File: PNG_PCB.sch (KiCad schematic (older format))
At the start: 2 parts, among them U1 screw_term, U2 Teensy4.1

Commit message: updated screw terminals to 2.54mm
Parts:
- removed U1: screw_term, Connector_PinHeader_1.27mm:PinHeader_1x02_P1.27mm_Vertical, symbol PNG_PCB_Parts:screw_term
- added J91: screw terminal, Connector_PinHeader_2.54mm:PinHeader_1x02_P2.54mm_Vertical, symbol Connector:Conn_01x02_Male
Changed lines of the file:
@@
 Text Label 3250 6450 2    50   ~ 0
 ADC_IN_9
-Wire Wire Line
-	5000 3250 4400 3250
-Text Label 4400 3250 0    50   ~ 0
+Text Label 5900 4300 2    50   ~ 0
 sync_in
-$Comp
-L PNG_PCB_Parts:screw_term U1
-U 1 1 601BAD2F
-P 5000 3250
-F 0 "U1" H 5058 3384 50  0000 L CNN
-F 1 "screw_term" H 5058 3293 50  0000 L CNN
-F 2 "Connector_PinHeader_1.27mm:PinHeader_1x02_P1.27mm_Vertical" H 5000 3250 50  0001 C CNN
-F 3 "" H 5000 3250 50  0001 C CNN
-	1    5000 3250
-	1    0    0    -1
-$EndComp
 Wire Wire Line
 	7300 1750 6700 1750
 Text Label 6700 1750 0    50   ~ 0
 sync_out
-Wire Wire Line
-	5000 3600 4400 3600
-Text Label 4400 3600 0    50   ~ 0
+Text Label 5900 4200 2    50   ~ 0
 sync_out
-$Comp
-L PNG_PCB_Parts:screw_term U1
-U 2 1 601BD94C
-P 5000 3600
-F 0 "U1" H 5058 3734 50  0000 L CNN
-F 1 "screw_term" H 5058 3643 50  0000 L CNN
-F 2 "Connector_PinHeader_1.27mm:PinHeader_1x02_P1.27mm_Vertical" H 5000 3600 50  0001 C CNN
-F 3 "" H 5000 3600 50  0001 C CNN
-	2    5000 3600
-	1    0    0    -1
-$EndComp
 NoConn ~ 9500 2950
 NoConn ~ 9500 3050
@@
 NoConn ~ 9500 3850
 NoConn ~ 9500 3950
+$Comp
+L Connector:Conn_01x02_Male J91
+U 1 1 601A940A
+P 5050 4200
+F 0 "J91" H 5158 4381 50  0000 C CNN
+F 1 "screw terminal" H 5158 4290 50  0000 C CNN
+F 2 "Connector_PinHeader_2.54mm:PinHeader_1x02_P2.54mm_Vertical" H 5050 4200 50  0001 C CNN
+F 3 "~" H 5050 4200 50  0001 C CNN
+	1    5050 4200
+	1    0    0    -1
+$EndComp
+Wire Wire Line
+	5250 4200 5900 4200
+Wire Wire Line
+	5250 4300 5900 4300
 $EndSCHEMATC

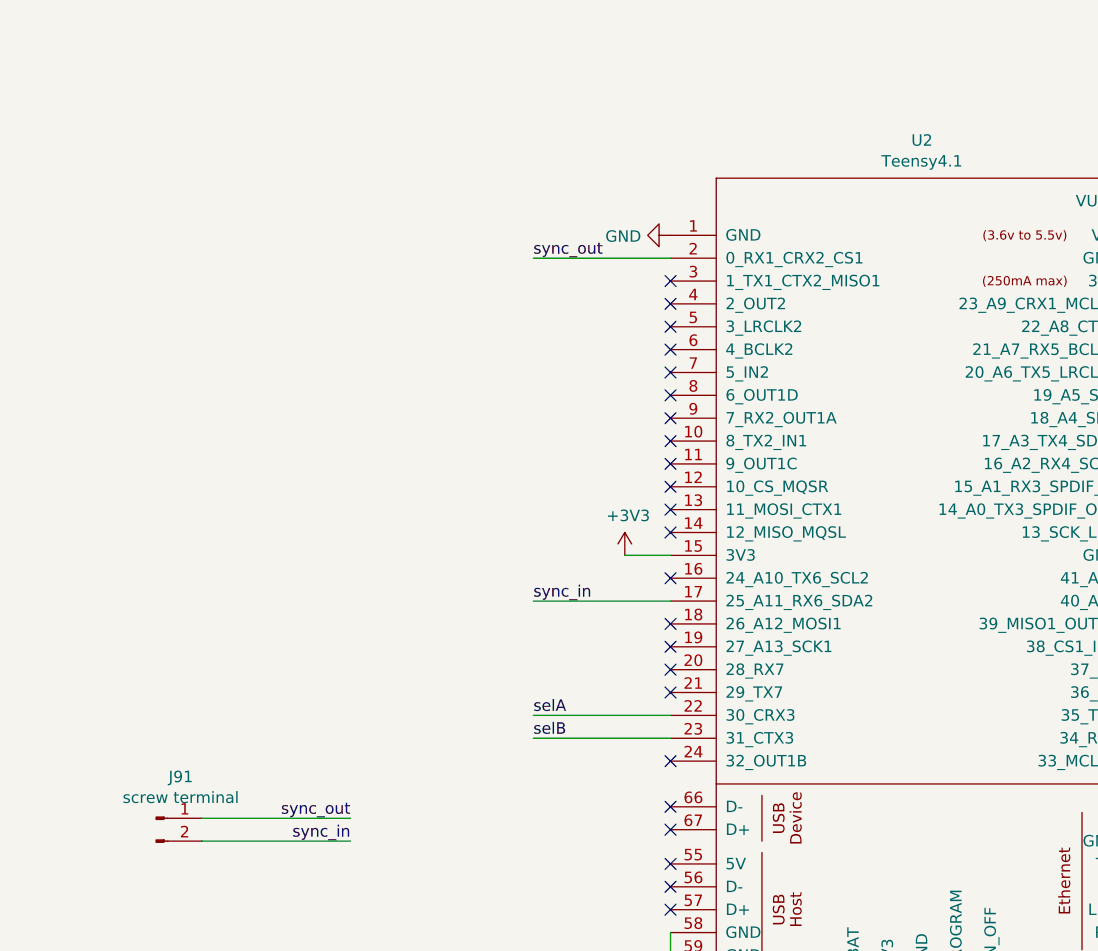
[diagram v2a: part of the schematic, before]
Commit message: revised sensor connector
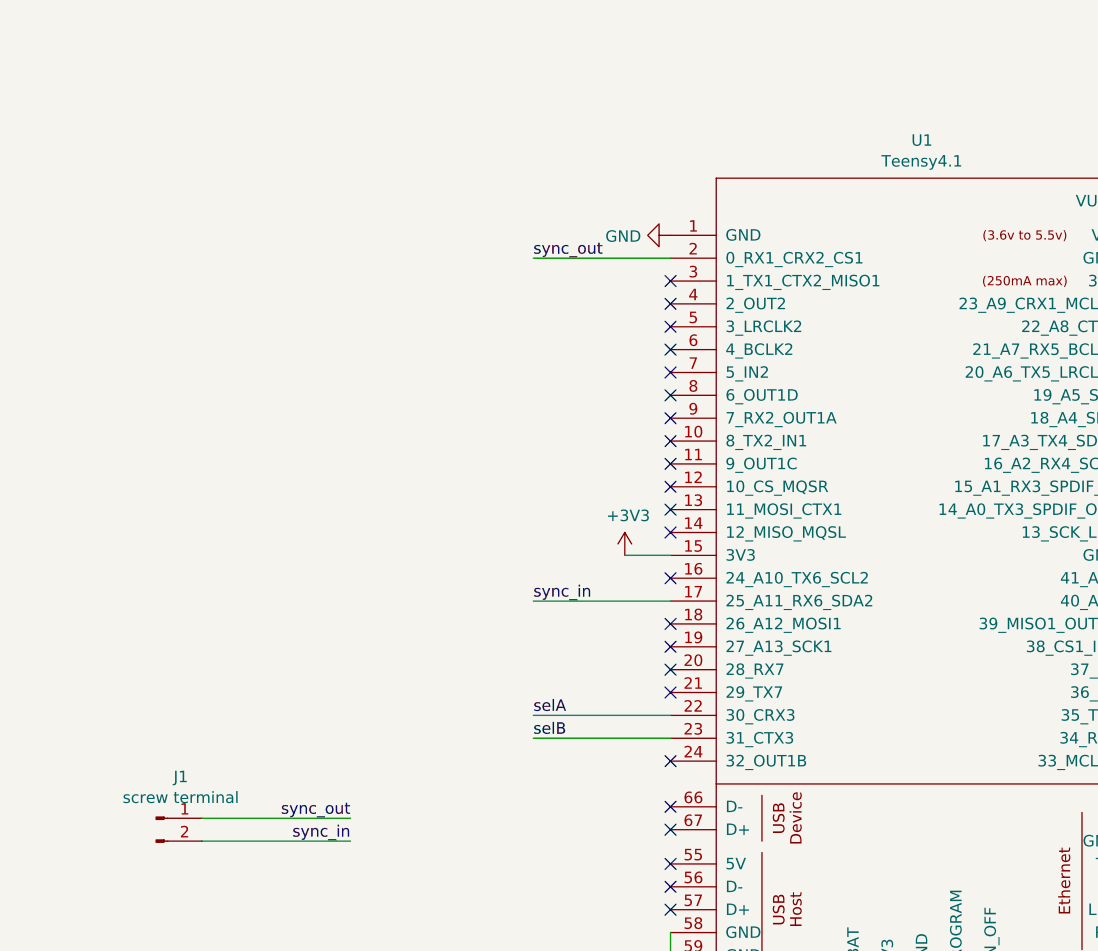
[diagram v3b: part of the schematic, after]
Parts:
- renumbered J91 to J1, U2 to U1
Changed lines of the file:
@@
 $EndDescr
 $Comp
-L teensy:Teensy4.1 U2
+L teensy:Teensy4.1 U1
 U 1 1 60133249
 P 8400 3800
-F 0 "U2" H 8400 6365 50  0000 C CNN
+F 0 "U1" H 8400 6365 50  0000 C CNN
 F 1 "Teensy4.1" H 8400 6274 50  0000 C CNN
 F 2 "teensy:Teensy41" H 8000 4200 50  0001 C CNN
@@
 NoConn ~ 9500 3950
 $Comp
-L Connector:Conn_01x02_Male J91
+L Connector:Conn_01x02_Male J1
 U 1 1 601A940A
 P 5050 4200
-F 0 "J91" H 5158 4381 50  0000 C CNN
+F 0 "J1" H 5158 4381 50  0000 C CNN
 F 1 "screw terminal" H 5158 4290 50  0000 C CNN
 F 2 "Connector_PinHeader_2.54mm:PinHeader_1x02_P2.54mm_Vertical" H 5050 4200 50  0001 C CNN

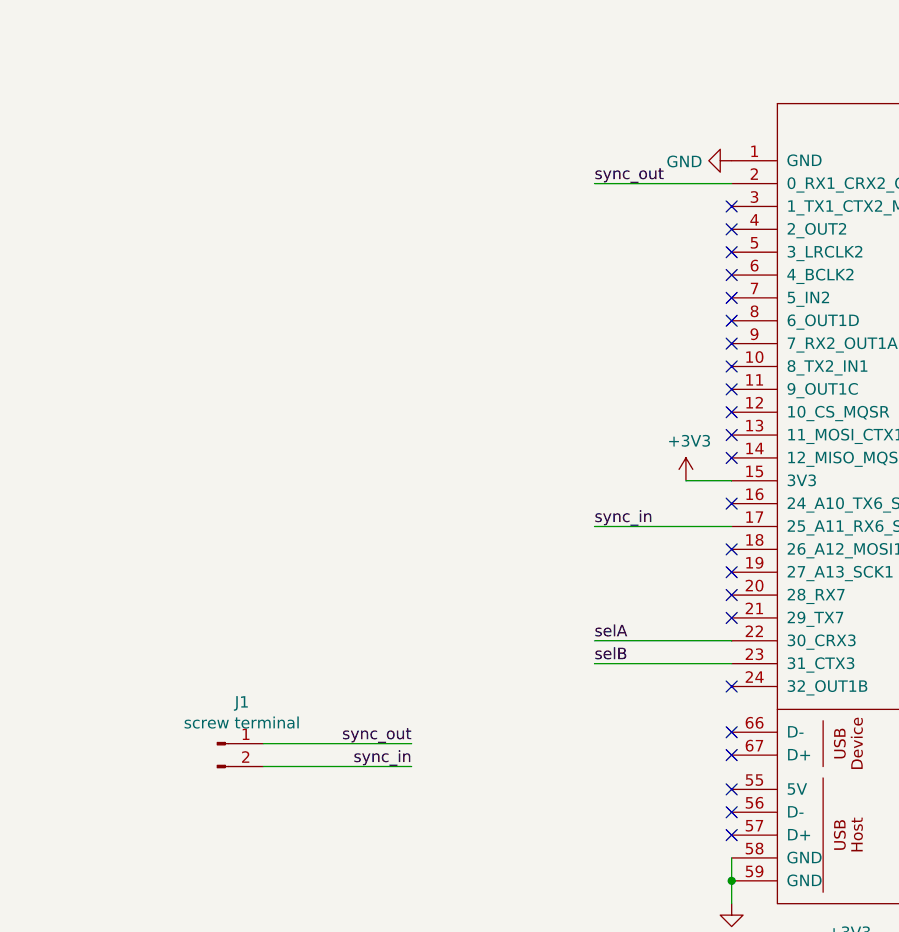
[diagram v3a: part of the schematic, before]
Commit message: removed sync signals
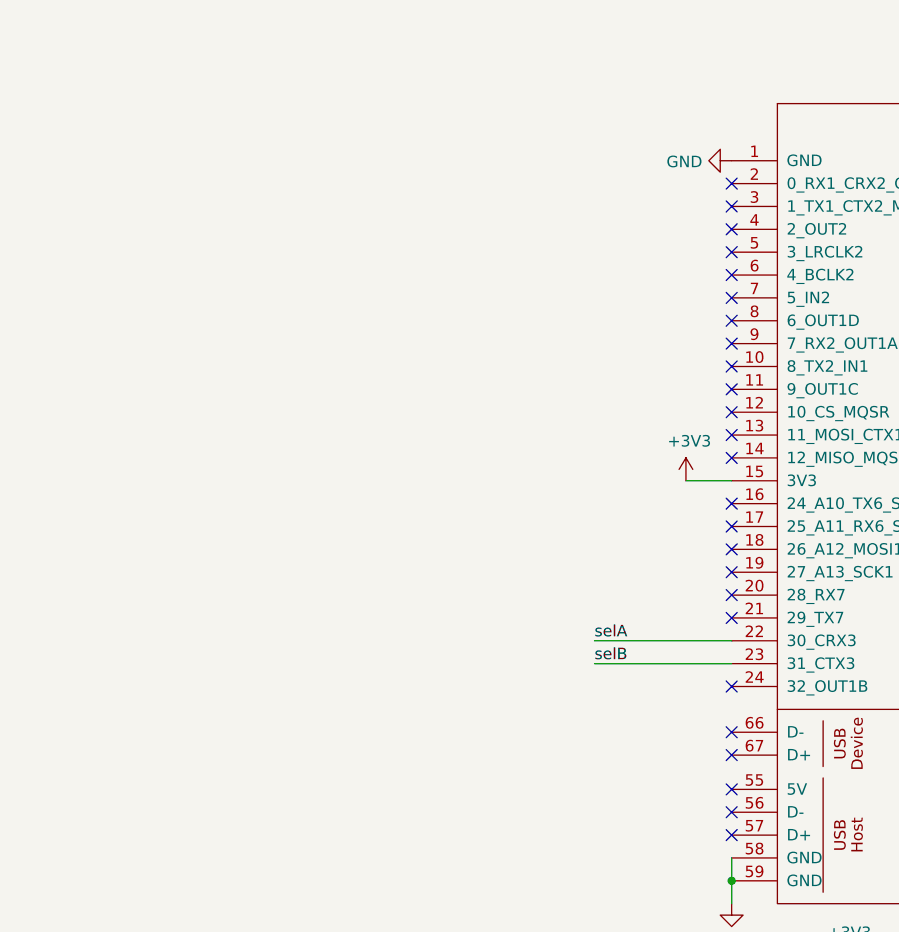
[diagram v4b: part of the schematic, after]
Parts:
- removed J1: screw terminal, Connector_PinHeader_2.54mm:PinHeader_1x02_P2.54mm_Vertical, symbol Connector:Conn_01x02_Male
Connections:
- net sync_in: no longer names the net of U1.17 (25_A11_RX6_SDA2)
- net sync_out: no longer names the net of U1.2 (0_RX1_CRX2_CS1)
- no-connect marks 45 -> 47
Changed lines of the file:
@@
 	7300 3050 7100 3050
 NoConn ~ 7300 3950
-Wire Wire Line
-	7300 3250 6700 3250
-Text Label 6700 3250 0    50   ~ 0
-sync_in
 Text Label 1150 850  0    50   ~ 0
 selA
@@
 Text Label 3250 6450 2    50   ~ 0
 ADC_IN_9
-Text Label 5900 4300 2    50   ~ 0
-sync_in
-Wire Wire Line
-	7300 1750 6700 1750
-Text Label 6700 1750 0    50   ~ 0
-sync_out
-Text Label 5900 4200 2    50   ~ 0
-sync_out
 NoConn ~ 9500 2950
 NoConn ~ 9500 3050
@@
 NoConn ~ 9500 3850
 NoConn ~ 9500 3950
-$Comp
-L Connector:Conn_01x02_Male J1
-U 1 1 601A940A
-P 5050 4200
-F 0 "J1" H 5158 4381 50  0000 C CNN
-F 1 "screw terminal" H 5158 4290 50  0000 C CNN
-F 2 "Connector_PinHeader_2.54mm:PinHeader_1x02_P2.54mm_Vertical" H 5050 4200 50  0001 C CNN
-F 3 "~" H 5050 4200 50  0001 C CNN
-	1    5050 4200
-	1    0    0    -1
-$EndComp
-Wire Wire Line
-	5250 4200 5900 4200
-Wire Wire Line
-	5250 4300 5900 4300
+NoConn ~ 7300 1750
+NoConn ~ 7300 3250
 $EndSCHEMATC
